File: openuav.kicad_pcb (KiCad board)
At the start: 4 copper layers, 36 x 36 mm, 85 parts, among them J1 Conn_01x01, J10 Conn_01x01, J11 Conn_01x01, J12 Conn_01x01, J13 Conn_01x01, J14 Conn_01x01, J15 Conn_01x01, J16 Conn_01x01, J17 Conn_01x01, J18 Conn_01x01, J19 Conn_01x01, J2 Conn_01x01, J20 Conn_01x01, J21 Conn_01x01, J22 Conn_01x01, J23 Conn_01x01, J24 Conn_01x01, J25 Conn_01x01, J3 Conn_01x01, J4 Conn_01x01, J5 Conn_01x01, J6 Conn_01x01, J7 Conn_01x01, J8 Conn_01x01, J9 Conn_01x01, J99 USB_C_Receptacle_USB2.0, SW1 SW_Push, SW2 SW_Push, U1 STM32G431CBUx, U2 LPS22HB, U3 LSM6DSR, U4 SY8303, U5 SY8303, U6 W25N01GVZEIG, U7 TLV75733PDBV

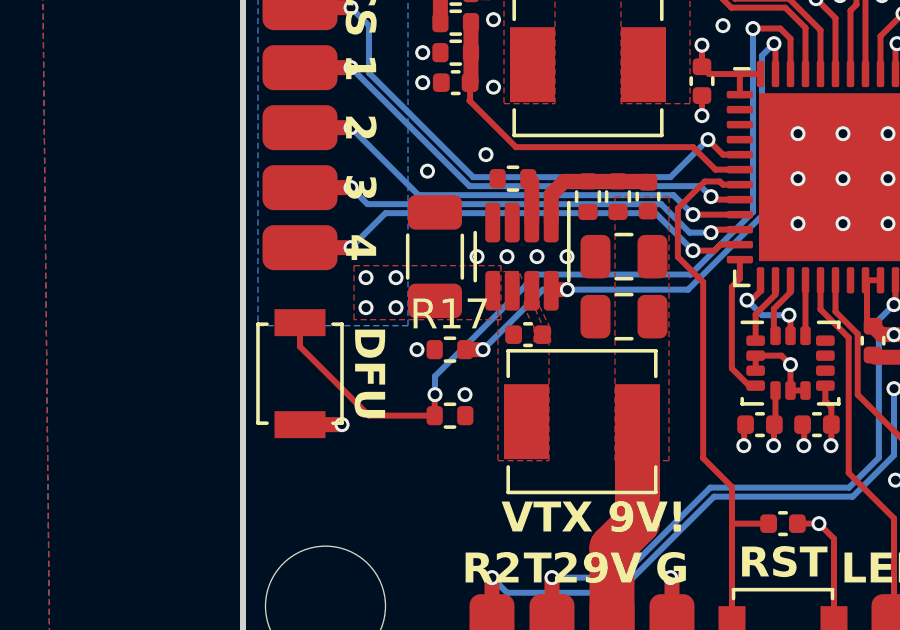
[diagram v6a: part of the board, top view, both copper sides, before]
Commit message: Update part number for baro
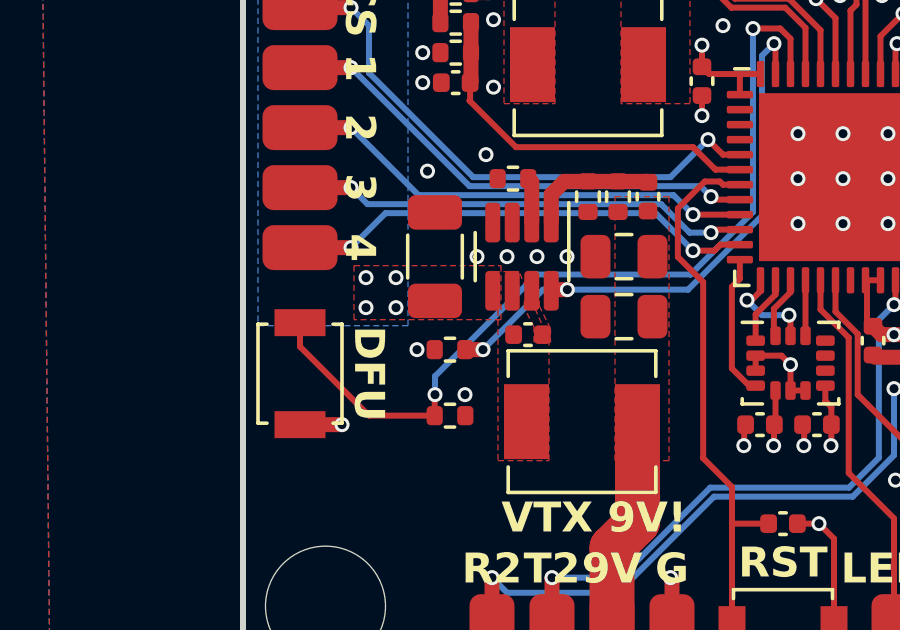
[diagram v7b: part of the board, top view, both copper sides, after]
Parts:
- U2: value LPS22HB -> LPS22HH
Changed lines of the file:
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@@
     (descr "ST  HLGA, 10 Pin (https://www.st.com/resource/en/datasheet/lps22hh.pdf#page=55), generated with kicad-footprint-generator ipc_noLead_generator.py")
     (tags "ST HLGA NoLead")
-    (property "LCSC" "C94049")
+    (property "LCSC" "C2827824")
     (property "Sheetfile" "openuav.kicad_sch")
     (property "Sheetname" "")
@@
         (effects (font (size 1 1) (thickness 0.15)))
     )
-    (fp_text value "LPS22HB" (at 0 1.95 90) (layer "F.Fab")
+    (fp_text value "LPS22HH" (at 0 1.95 90) (layer "F.Fab")
         (effects (font (size 1 1) (thickness 0.15)))
     )
@@
     (property "ki_keywords" "R resistor")
     (attr smd)
-    (fp_text reference "R17" (at 0 -1.17) (layer "F.SilkS")
-        (effects (font (size 1 1) (thickness 0.15)))
-    )
+    (fp_text reference "R17" (at 0 -1.17) (layer "F.SilkS") hide
+        (effects (font (size 1 1) (thickness 0.15)))
+    )
